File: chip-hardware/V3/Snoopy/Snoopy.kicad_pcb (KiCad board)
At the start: 2 copper layers, 0 parts

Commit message: Started adding peices onto pcb
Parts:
- added C1: 10uF, Capacitor_SMD:C_0603_1608Metric_Pad1.08x0.95mm_HandSolder, F.Cu at (156.2, 114.4)
- added C2: 1uF, Capacitor_SMD:C_0603_1608Metric_Pad1.08x0.95mm_HandSolder, F.Cu at (151.9, 114.4)
- added J1: Screw_Terminal_01x02, TerminalBlock_RND:TerminalBlock_RND_205-00232_1x02_P5.08mm_Horizontal, F.Cu at (194.4, 86.1)
- added J2: KLDX-0202-B, KLDX-0202-B:Kycon-KLDX-0202-B-MFG, F.Cu at (153.8, 78.9)
- added J3: 501461-0491, 5014610491:Molex-501461-0491-Manufacturer_Recommended, F.Cu at (187.9, 94.5)
- added J4: Conn_01x02, Connector_Wago:Wago_734-162_1x02_P3.50mm_Horizontal, F.Cu at (172.1, 89.3)
- added R1: 10k, Resistor_SMD:R_0603_1608Metric_Pad0.98x0.95mm_HandSolder, F.Cu at (193.0, 92.4)
- added R2: 10k, Resistor_SMD:R_0603_1608Metric_Pad0.98x0.95mm_HandSolder, F.Cu at (151.9, 116.9)
- added R3: 10k, Resistor_SMD:R_0603_1608Metric_Pad0.98x0.95mm_HandSolder, F.Cu at (156.2, 116.9)
- added R4: 10k, Resistor_SMD:R_0603_1608Metric_Pad0.98x0.95mm_HandSolder, F.Cu at (205.2, 81.9)
- added U1: INA260, Package_SO:TSSOP-16_4.4x5mm_P0.65mm, F.Cu at (178.5, 107.5)
- added U2: TLV70033_SOT23-5, Package_TO_SOT_SMD:SOT-23-5, F.Cu at (147.1, 115.4)
- added U3: ESP32-WROOM-32, RF_Module:ESP32-WROOM-32, F.Cu at (134.7, 81.3)
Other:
- board outline added: 43.7 x 28 mm

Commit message: Added adjustment to the PCB. Everything seems right
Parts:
- J4: footprint Connector_Wago:Wago_734-162_1x02_P3.50mm_Horizontal -> Connector_Wire:SolderWire-0.1sqmm_1x02_P3.6mm_D0.4mm_OD1mm
- moved J1 80.0 mm to (114.6, 91.5)
- moved J3 78.5 mm to (110.2, 83.6), turned to -90 degrees
- moved U1 66.8 mm to (119.5, 76.2), turned to -90 degrees
- moved J4 27.3 mm to (149.3, 74.4)
- moved R1 24.2 mm to (176.1, 109.7)
- moved R4 24.2 mm to (188.3, 99.2)
- moved U2 23.1 mm to (152.9, 93.0), turned to 180 degrees
- moved J2 4.75 mm to (153.7, 83.6)
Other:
- board size 43.7 x 28 mm -> 49.8 x 29.2 mm

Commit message: got placement down
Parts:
- moved R4 55.7 mm to (132.7, 95.9)
- moved R1 50.1 mm to (127.9, 95.9)
- moved R2 50.0 mm to (115.9, 82.2)
- moved R3 48.8 mm to (121.9, 82.3)
- moved C2 23.2 mm to (137.9, 96.0), turned to 90 degrees
- moved C1 23.1 mm to (142.4, 95.9), turned to 90 degrees
- moved U2 4.44 mm to (148.5, 92.6)
- moved U1 1.45 mm to (118.1, 75.7), turned to 0 degrees
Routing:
- net (no net): vias 0 -> 2
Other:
- outline, holes or cut-outs redrawn

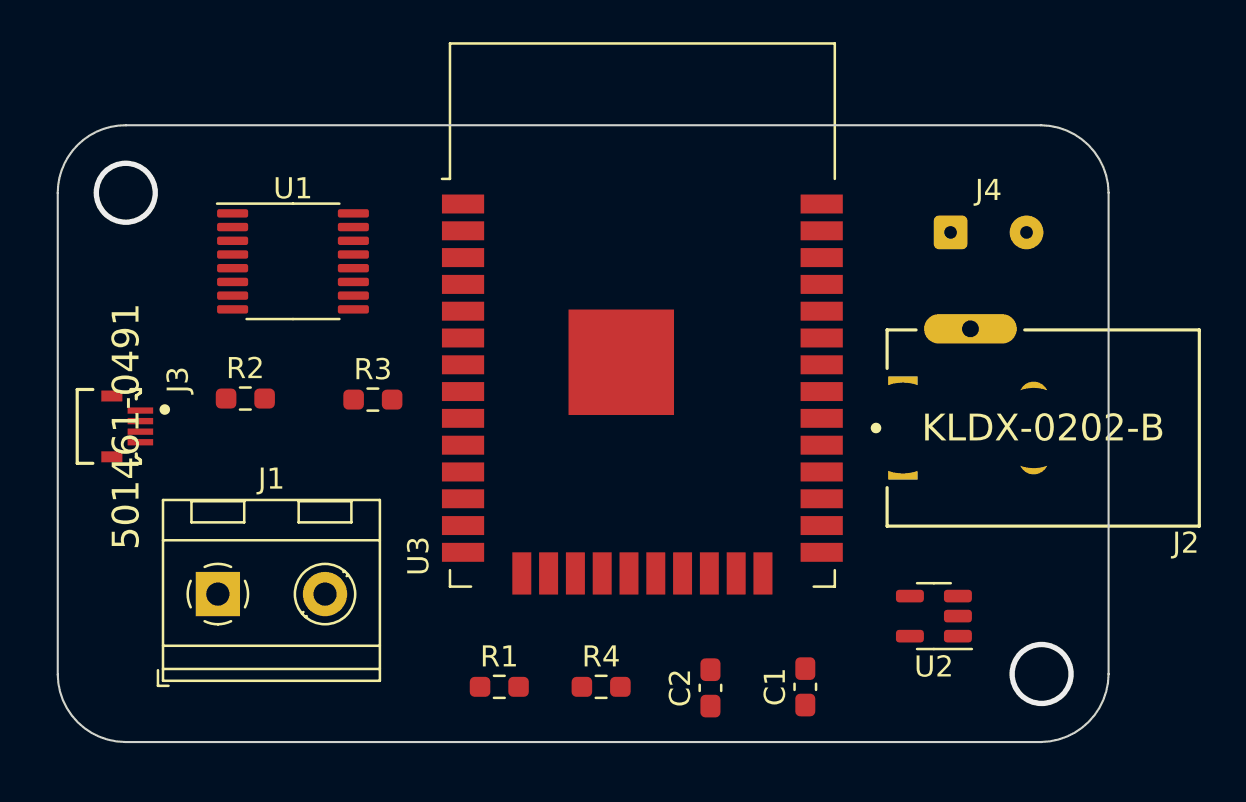
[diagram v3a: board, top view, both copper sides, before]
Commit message: finished second board with some minor errors
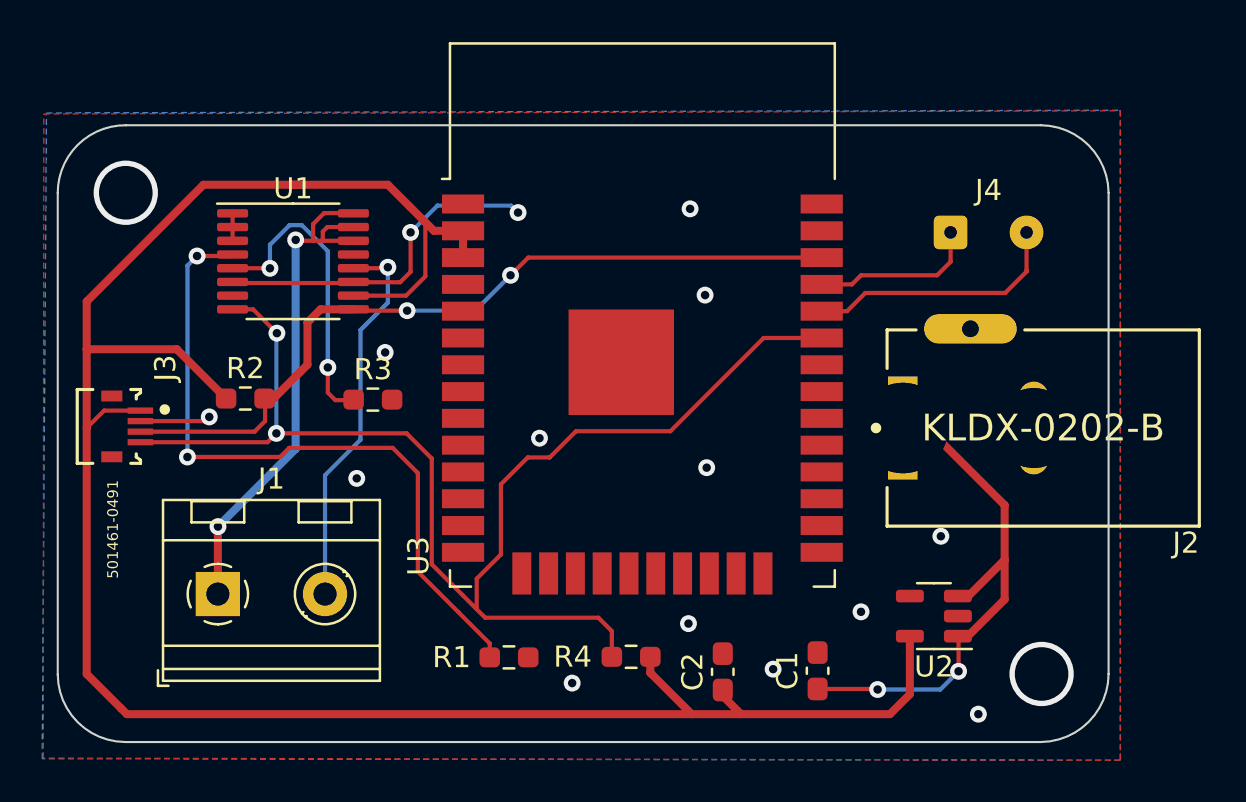
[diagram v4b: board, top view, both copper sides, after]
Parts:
- moved R4 2.01 mm to (134.2, 94.5), turned to 180 degrees
- moved R1 1.47 mm to (128.4, 94.5)
- moved C1 0.96 mm to (143.0, 95.1)
- moved C2 0.96 mm to (138.5, 95.2)
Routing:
- net +3V3: track 0.00 -> 105.3 mm
- net /SDA: track 0.00 -> 62.4 mm, vias 0 -> 2
- net /SCL: track 0.00 -> 37.6 mm, vias 0 -> 2
- net Net-(R1-Pad1): track 0.00 -> 33.2 mm, vias 0 -> 2
- net Net-(J1-Pad1): track 0.00 -> 26.0 mm, vias 0 -> 2
- net Net-(C1-Pad1): track 0.00 -> 25.4 mm, vias 0 -> 2
- net GND: track 0.00 -> 19.7 mm, vias 0 -> 15
- net Net-(J1-Pad2): track 0.00 -> 18.4 mm, vias 0 -> 1
- net Net-(R3-Pad1): track 0.00 -> 14.6 mm, vias 0 -> 2
- net Net-(J4-Pad2): track 0.00 -> 12.4 mm
- net Net-(J4-Pad1): track 0.00 -> 7.95 mm
- net Net-(U1-Pad1): track 0.00 -> 1.30 mm
- added copper zone on B.Cu, net GND
- added copper zone on F.Cu, net GND
